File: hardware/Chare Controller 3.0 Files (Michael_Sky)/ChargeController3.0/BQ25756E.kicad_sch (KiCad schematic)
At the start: 16 parts, among them U1 BQ25756ERRVR

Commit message: push test
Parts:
- added J1, J12: Conn_02x26_Odd_Even, symbol Connector_Generic:Conn_02x26_Odd_Even
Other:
- moved on the sheet: C22, C23, C3, C4, C6, C7, R4, R_AC1, R_AC2, R_AC3, R_FB1, R_FBG1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

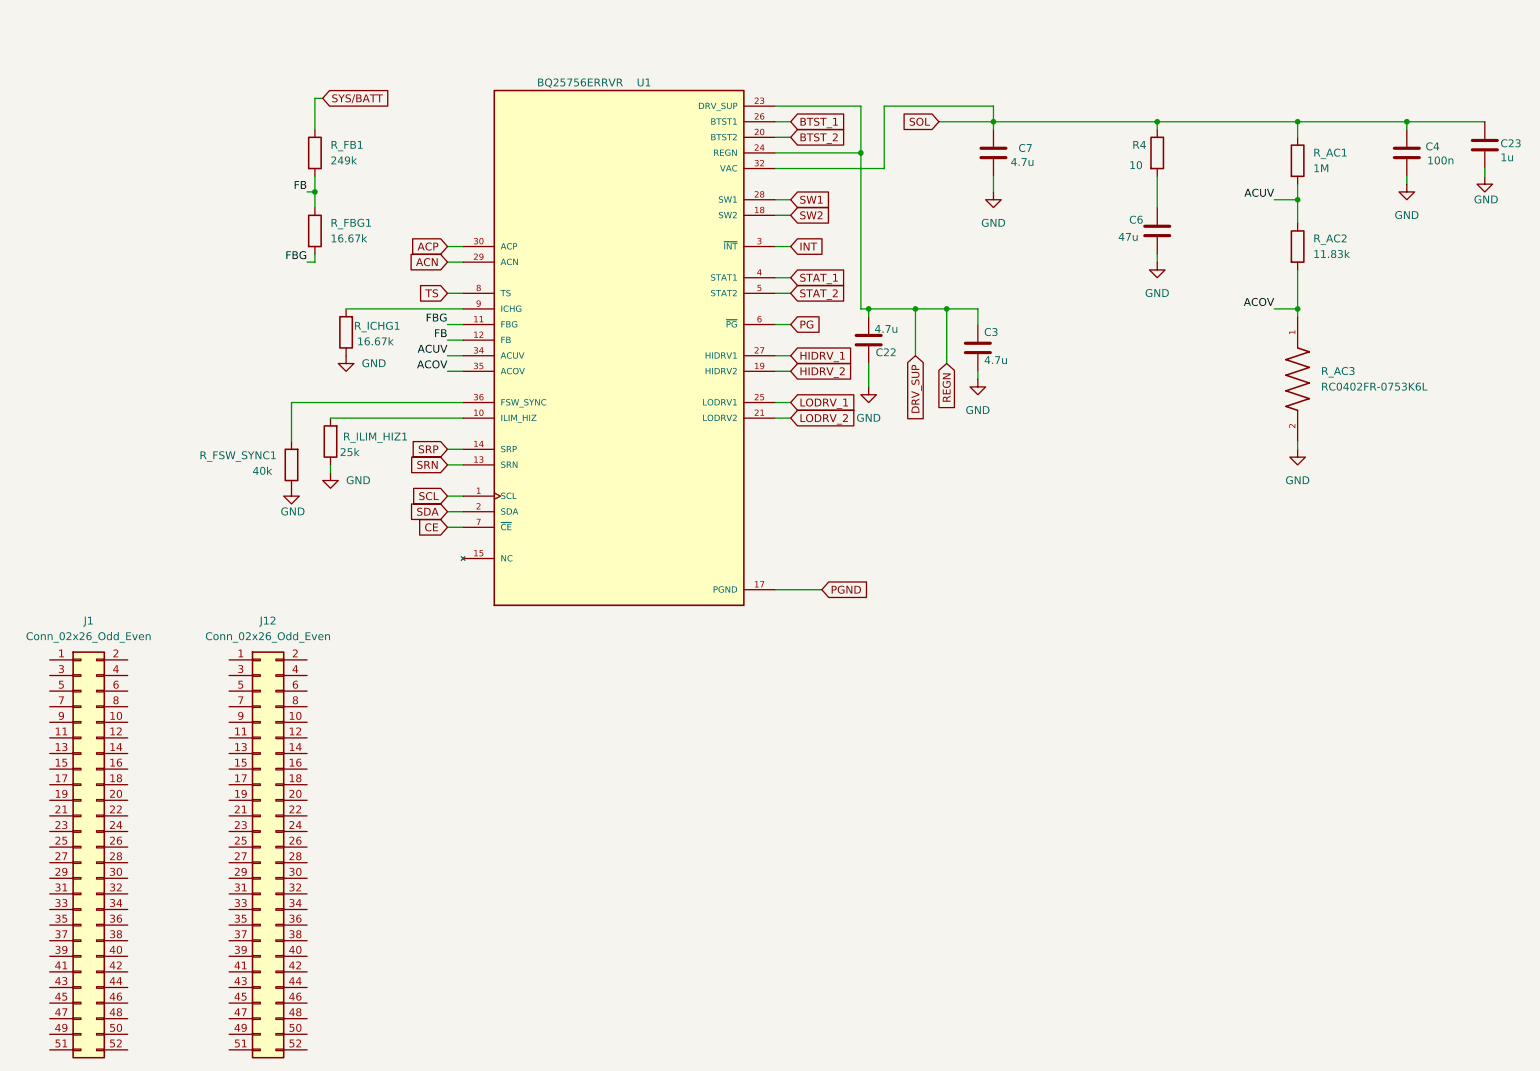
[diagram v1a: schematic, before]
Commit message: Added header pins and started labelling outputs
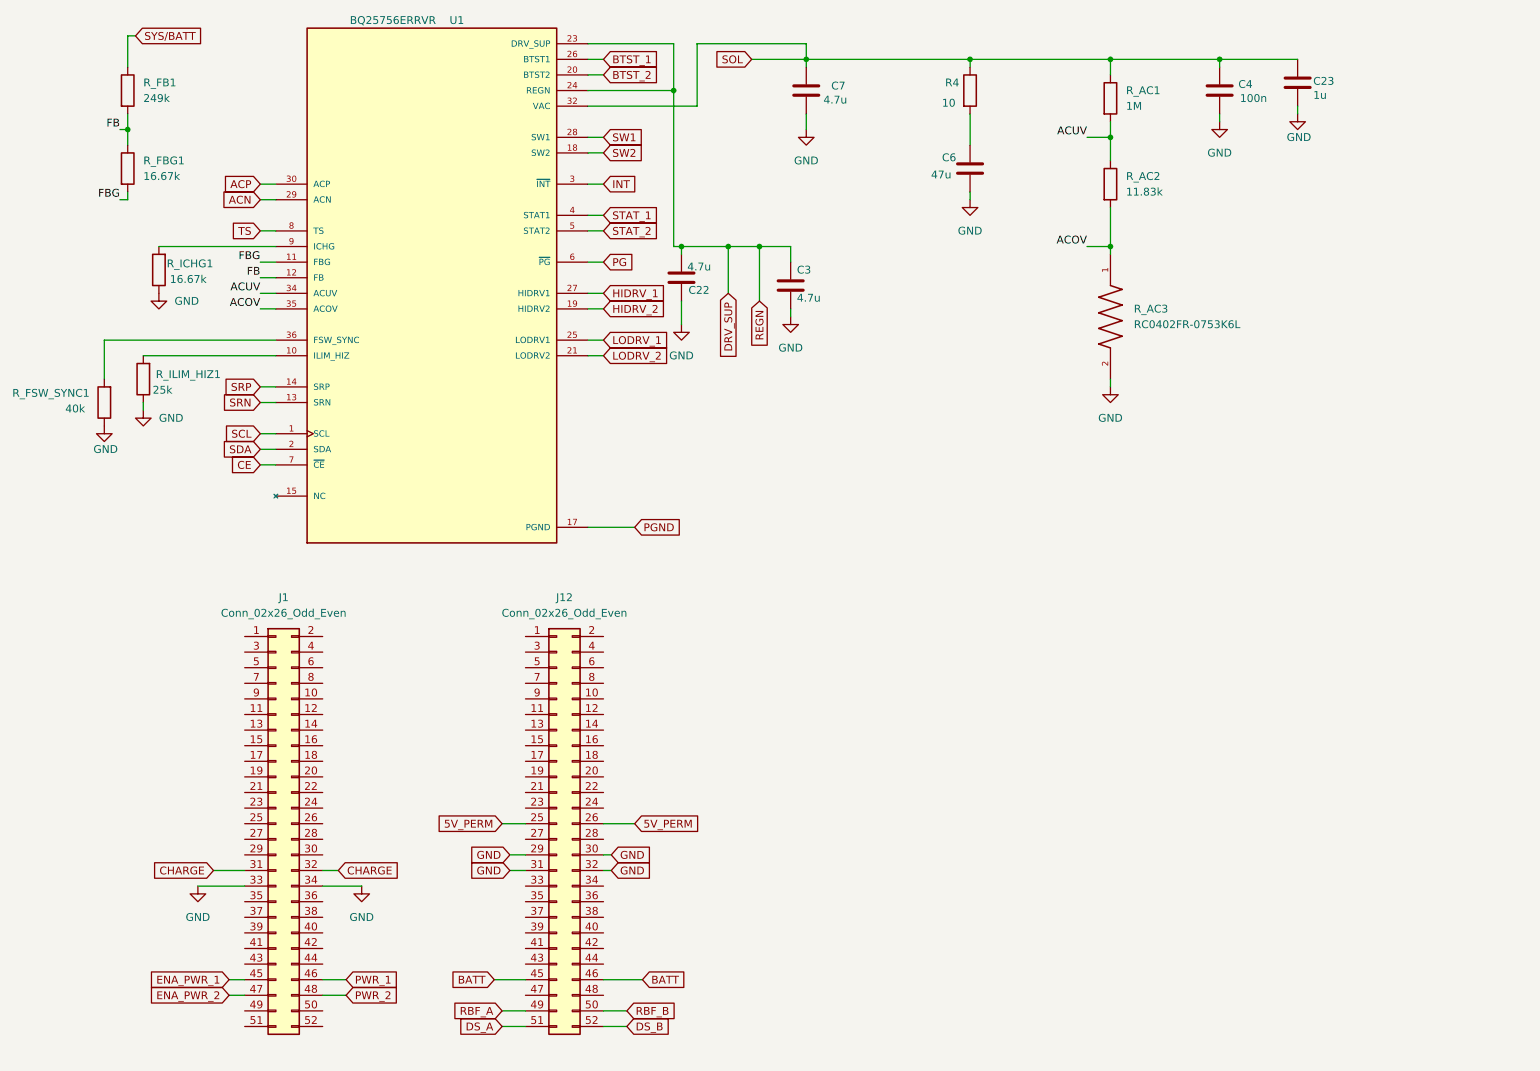
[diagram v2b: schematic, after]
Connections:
- net GND: now also J1.33 (Pin_33), J1.34 (Pin_34), J12.29 (Pin_29), J12.30 (Pin_30), J12.31 (Pin_31), J12.32 (Pin_32)
- net 5V_PERM: now reaches J12.25 (Pin_25)
- net 5V_PERM: now also J12.26 (Pin_26)
- net BATT: now reaches J12.45 (Pin_45)
- net BATT: now also J12.46 (Pin_46)
- net RBF_A: now reaches J12.49 (Pin_49)
- net RBF_B: now reaches J12.50 (Pin_50)
- net DS_A: now reaches J12.51 (Pin_51)
- net DS_B: now reaches J12.52 (Pin_52)
- net CHARGE: now reaches J1.31 (Pin_31)
- net CHARGE: now also J1.32 (Pin_32)
- net ENA_PWR_1: now reaches J1.45 (Pin_45)
- net PWR_1: now reaches J1.46 (Pin_46)
- net ENA_PWR_2: now reaches J1.47 (Pin_47)
- net PWR_2: now reaches J1.48 (Pin_48)
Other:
- moved on the sheet: C22, C23, C3, C4, C6, C7, J1, J12, R4, R_AC1, R_AC2, R_AC3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

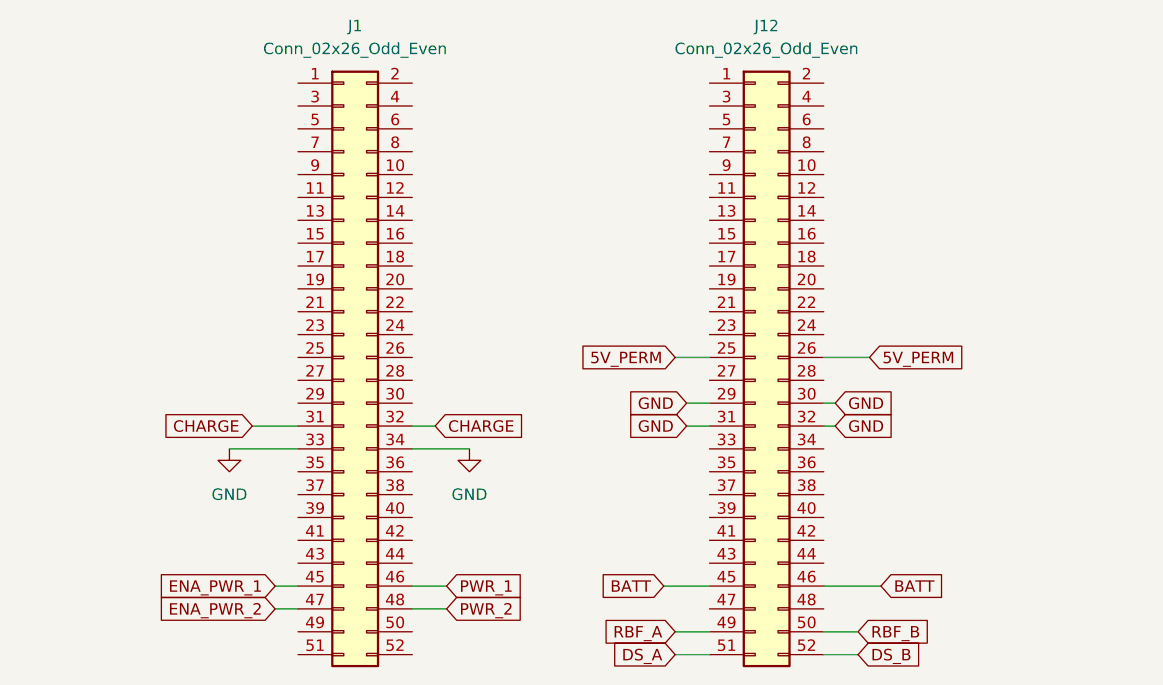
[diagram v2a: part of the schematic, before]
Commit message: more label placement
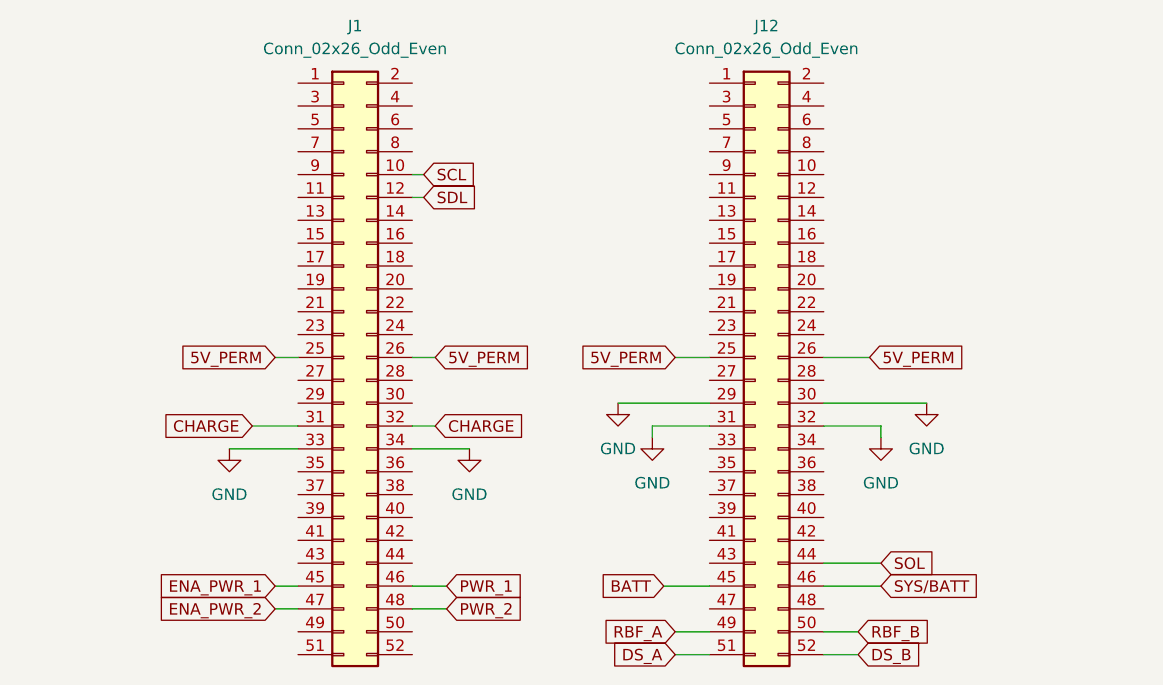
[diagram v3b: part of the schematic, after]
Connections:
- net 5V_PERM: now also J1.25 (Pin_25), J1.26 (Pin_26)
- net BATT: no longer J12.46 (Pin_46)
- net SCL: now also J1.10 (Pin_10)
- net SYS/BATT: now also J12.46 (Pin_46)
- net VAC: now also J12.44 (Pin_44)
- net SDL: now reaches J1.12 (Pin_12)

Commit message: Formatting
Added schematic template from librecube, attempted to fix footprint template file path issues by copying over footprints into current project library
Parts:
- J1, J12: footprint (none) -> Connector_PinSocket_2.54mm:PinSocket_2x26_P2.54mm_Vertical
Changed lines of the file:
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@@
 			)
 		)
-		(property "Footprint" ""
+		(property "Footprint" "Connector_PinSocket_2.54mm:PinSocket_2x26_P2.54mm_Vertical"
 			(at 111.76 151.13 0)
 			(effects
@@
 			)
 		)
-		(property "Footprint" ""
+		(property "Footprint" "Connector_PinSocket_2.54mm:PinSocket_2x26_P2.54mm_Vertical"
 			(at 66.04 151.13 0)
 			(effects

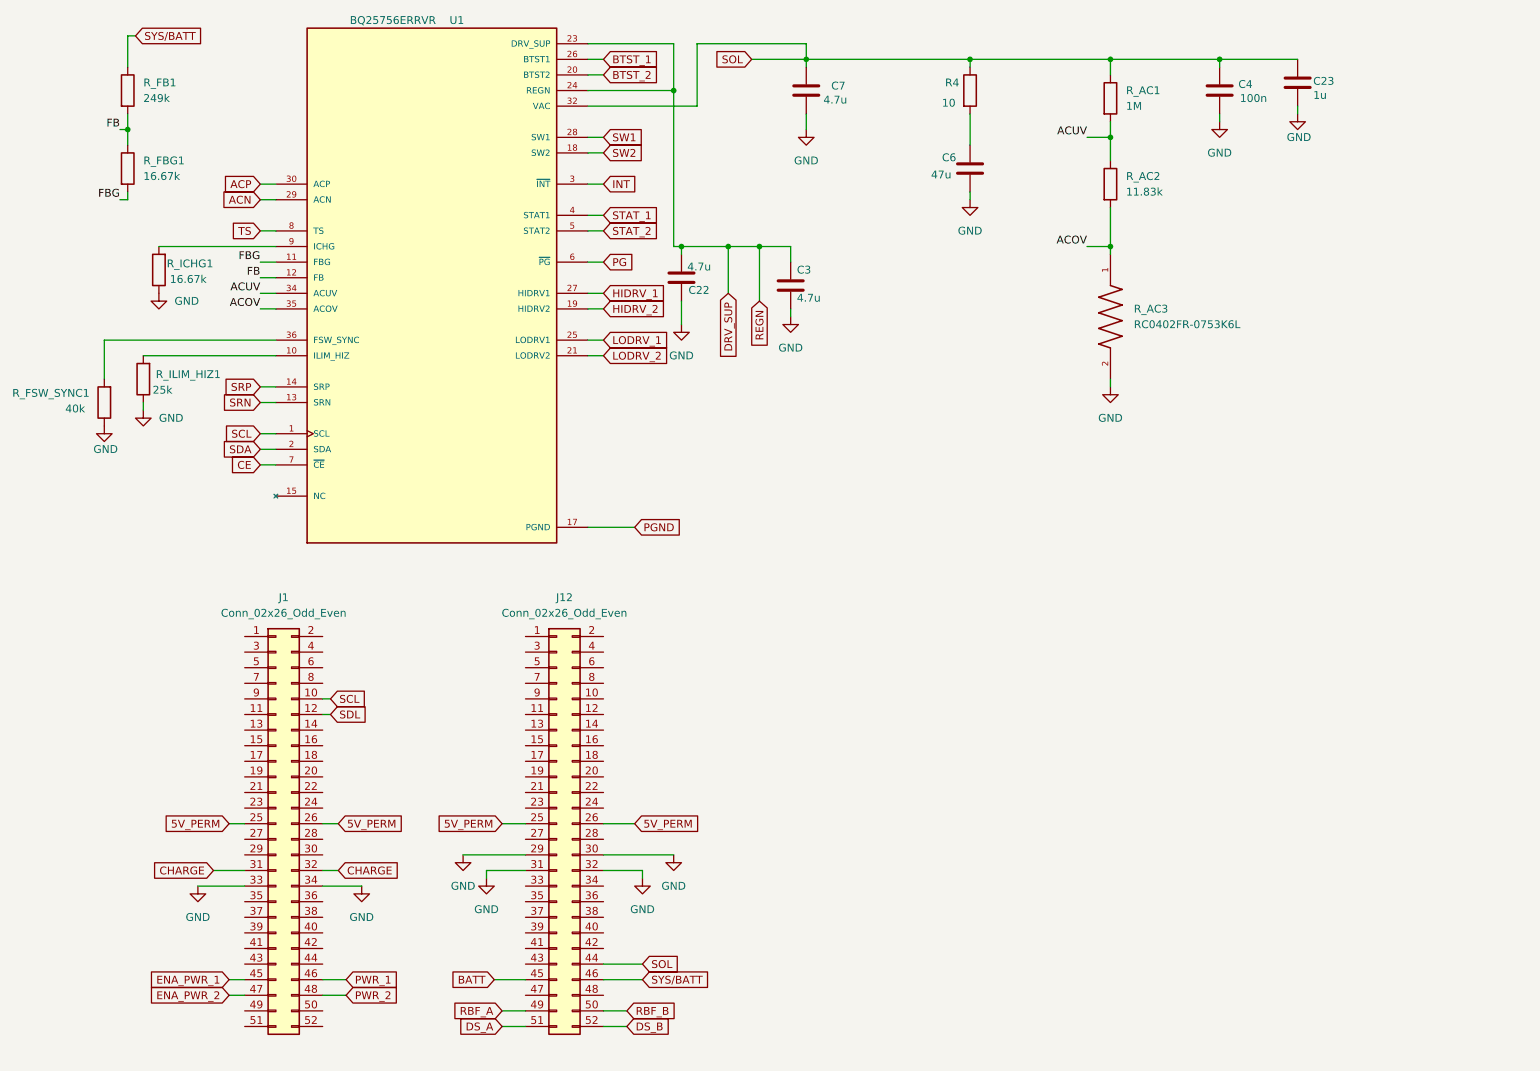
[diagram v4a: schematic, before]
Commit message: moved pins to sep page
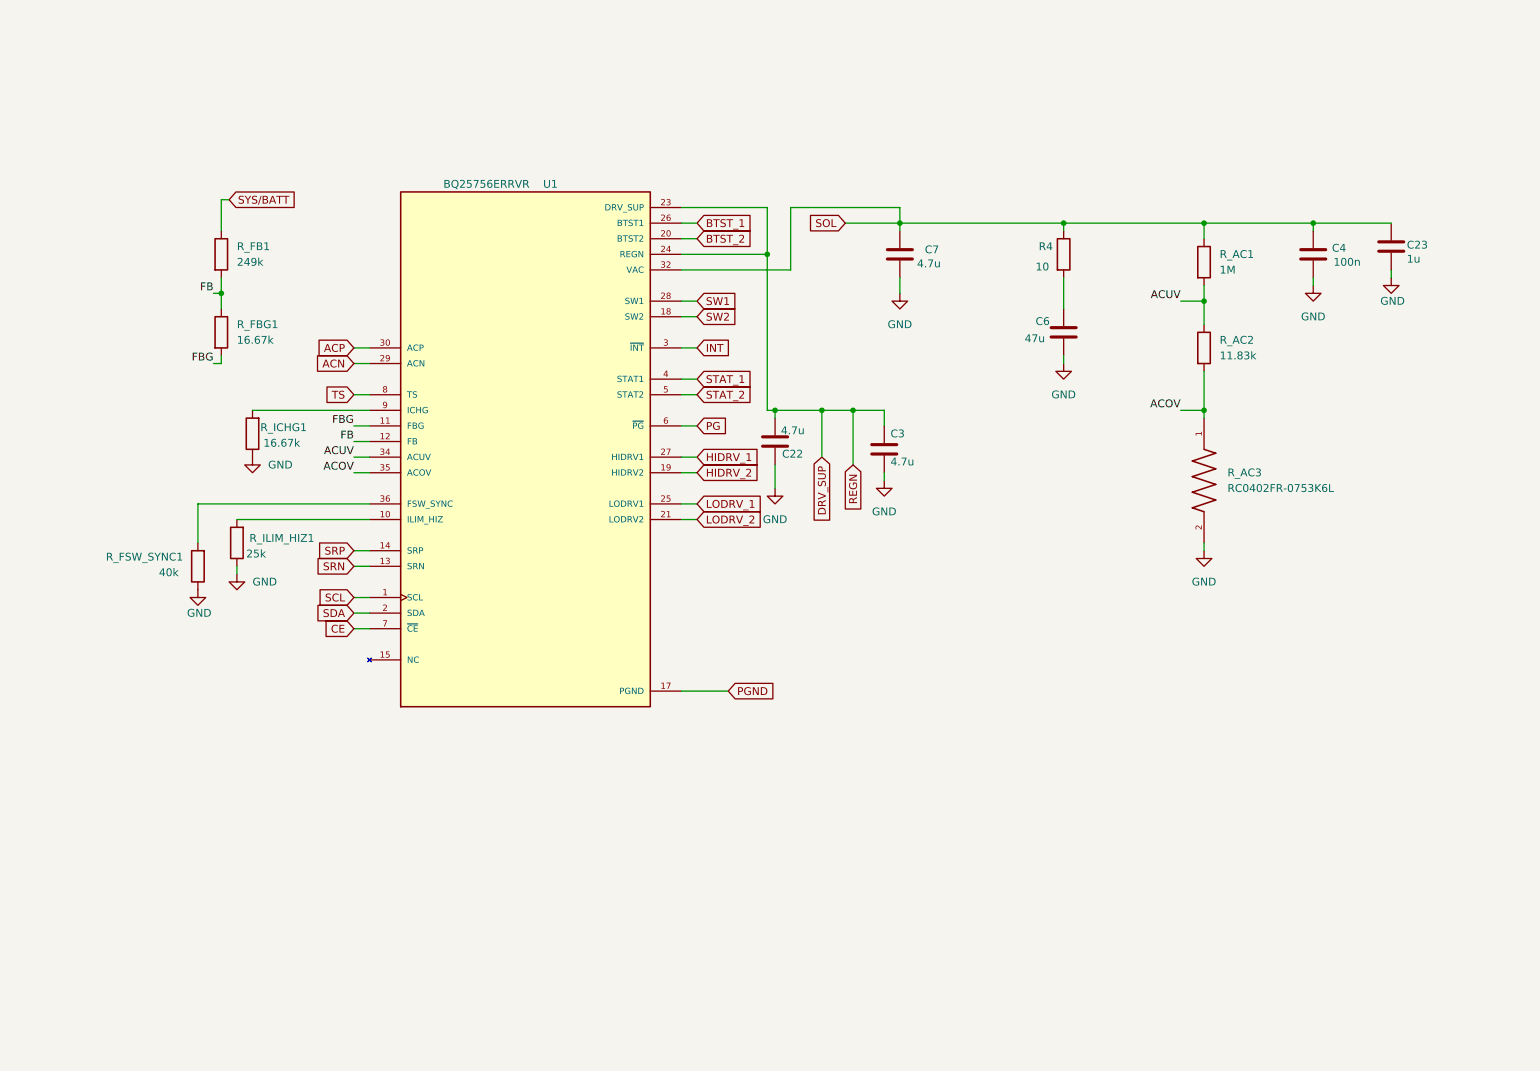
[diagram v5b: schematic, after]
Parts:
- removed J1, J12: Conn_02x26_Odd_Even, Connector_PinSocket_2.54mm:PinSocket_2x26_P2.54mm_Vertical, symbol Connector_Generic:Conn_02x26_Odd_Even
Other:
- moved on the sheet: C22, C23, C3, C4, C6, C7, R4, R_AC1, R_AC2, R_AC3, R_FB1, R_FBG1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
